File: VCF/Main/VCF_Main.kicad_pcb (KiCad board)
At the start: 2 copper layers, 39.6 x 74.4 mm, 46 parts, among them J1 Power, J2 Power, U1 TL072, U2 TL072, U3 AS3320

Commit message: Clean up VCF boards
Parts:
- added REF**: OSHW-Logo2_7.3x6mm_SilkScreen, Symbol:OSHW-Logo2_7.3x6mm_SilkScreen, B.Cu at (69.6, 102.4)
- moved J2 2.79 mm to (67.8, 126.0)
- moved R3 1.02 mm to (99.8, 131.8)
- moved R2 0.51 mm to (99.8, 129.8)
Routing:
- net +12V: track 80.9 -> 82.6 mm
- net -12V: track 149.0 -> 150.2 mm
- net /In_3: track 22.7 -> 21.6 mm
- net Net-(R1-Pad1): track 19.5 -> 18.9 mm
- net GNDREF: vias 0 -> 4
- net (no net): vias 4 -> 0
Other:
- board size 39.6 x 74.4 mm -> 39.6 x 75.2 mm
- board text added: "+12V"
- board text added: "-12V"
- board text added: "Cutoff"
- board text added: "CutoffM"
- board text added: "In 1"
- board text added: "In 2"
- board text added: "In 3"
- board text added: "Out"
- board text added: "Res"
- board text added: "ResM"
- board text added: "VCF Main Board Rev 2"
- board text added: "WH"
- board text removed: "VCF Board Rev 2"
- board text removed: "WHSynth"

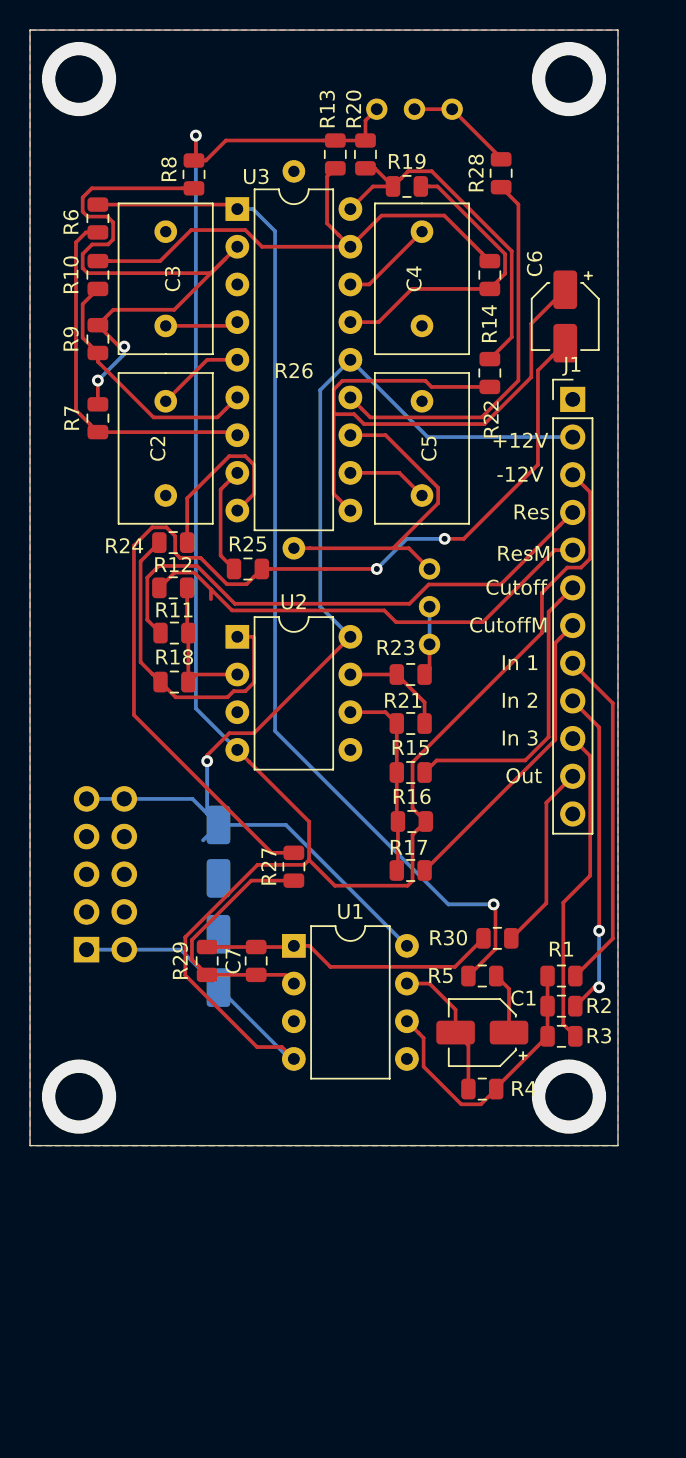
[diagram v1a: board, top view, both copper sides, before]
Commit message: Fix inverted resonance control input
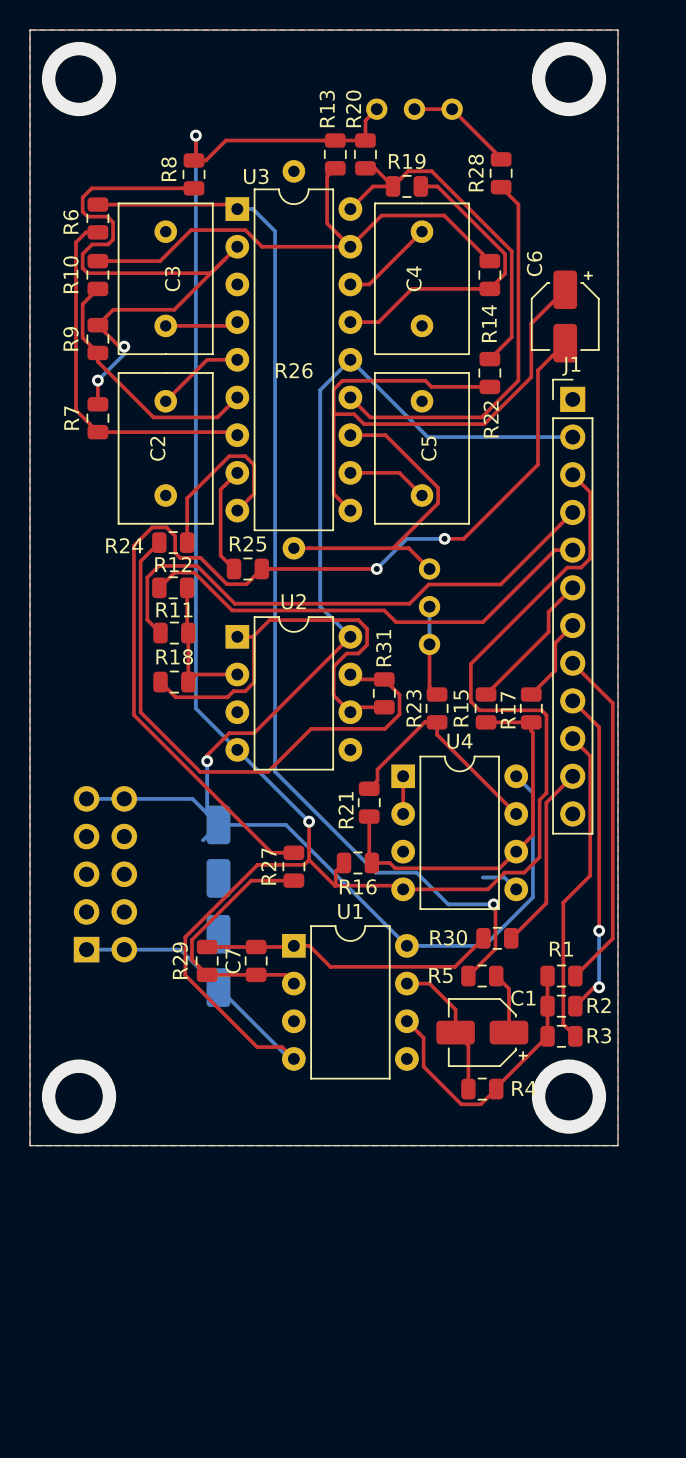
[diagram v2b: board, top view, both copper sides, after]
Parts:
- added R31: 100K, Resistor_SMD:R_0805_2012Metric, F.Cu at (87.9, 108.7)
- added U4: TL072, Package_DIP:DIP-8_W7.62mm, F.Cu at (89.2, 114.3)
- moved R17 13.6 mm to (97.8, 109.7), turned to 90 degrees
- moved R15 6.67 mm to (94.7, 109.7), turned to 90 degrees
- moved R21 6.02 mm to (86.9, 116.1), turned to 270 degrees
- moved R16 4.58 mm to (86.1, 120.1), turned to 180 degrees
- moved R23 2.90 mm to (91.4, 109.7), turned to 270 degrees
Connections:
- R24 pad 2: Net-(R18-Pad1) -> Net-(R24-Pad2)
- U2 pad 6: Net-(R15-Pad1) -> Net-(R18-Pad1)
- U2 pad 7: Net-(R21-Pad1) -> Net-(R24-Pad2)
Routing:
- net Net-(R24-Pad2): track 0.00 -> 37.9 mm
- net +12V: track 82.6 -> 101.1 mm
- net /Cutoff_Mod: track 20.6 -> 5.81 mm
- net Net-(R15-Pad1): track 13.4 -> 25.8 mm
- net -12V: track 150.2 -> 162.5 mm, vias 1 -> 2
- net /Cutoff: track 20.1 -> 9.61 mm
- net Net-(R21-Pad1): track 7.21 -> 15.2 mm
- net Net-(R18-Pad1): track 21.9 -> 29.7 mm
- net GNDREF: track 0.00 -> 2.58 mm
- net Net-(U4-Pad1): track 0.00 -> 2.54 mm
- net Net-(R5-Pad1): track 71.6 -> 73.2 mm
- net Net-(R23-Pad1): track 4.71 -> 6.13 mm
- net /Res_Mod: track 32.3 -> 31.7 mm
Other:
- board text removed: "+12V"
- board text removed: "-12V"
- board text removed: "Cutoff"
- board text removed: "CutoffM"
- board text removed: "In 1"
- board text removed: "In 2"
- board text removed: "In 3"
- board text removed: "Out"
- board text removed: "Res"
- board text removed: "ResM"

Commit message: Bunch of bug fixes and tweaks
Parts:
- added C10: C, Capacitor_SMD:C_0805_2012Metric, F.Cu at (91.9, 136.0)
- added C11: C, Capacitor_SMD:C_0805_2012Metric, F.Cu at (71.0, 106.3)
- added C12: C, Capacitor_SMD:C_0805_2012Metric, F.Cu at (83.4, 116.1)
- added C13: C, Capacitor_SMD:C_0805_2012Metric, F.Cu at (73.8, 111.4)
- added H1: Top_MH1, Eurorack:eurorack_mounting_hole, F.Cu at (67.3, 67.3)
- added H2: Bottom_MH1, Eurorack:eurorack_mounting_hole, F.Cu at (67.3, 135.9)
- added H3: Top_MH2, Eurorack:eurorack_mounting_hole, F.Cu at (100.3, 67.3)
- added H4: Bottom_MH2, Eurorack:eurorack_mounting_hole, F.Cu at (100.3, 135.9)
- moved R4 1.20 mm to (95.5, 136.0), turned to 270 degrees
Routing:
- net Net-(C11-Pad2): track 29.7 -> 35.3 mm
- net Net-(C13-Pad2): track 37.9 -> 42.9 mm
- net Net-(C11-Pad1): track 9.89 -> 14.1 mm
- net Net-(C12-Pad2): track 15.2 -> 18.7 mm
- net Net-(C1-Pad2): track 9.72 -> 13.0 mm
- net Net-(C10-Pad1): track 18.9 -> 21.3 mm
- net Net-(C6-Pad2): track 68.3 -> 70.4 mm
- net GNDREF: vias 4 -> 0

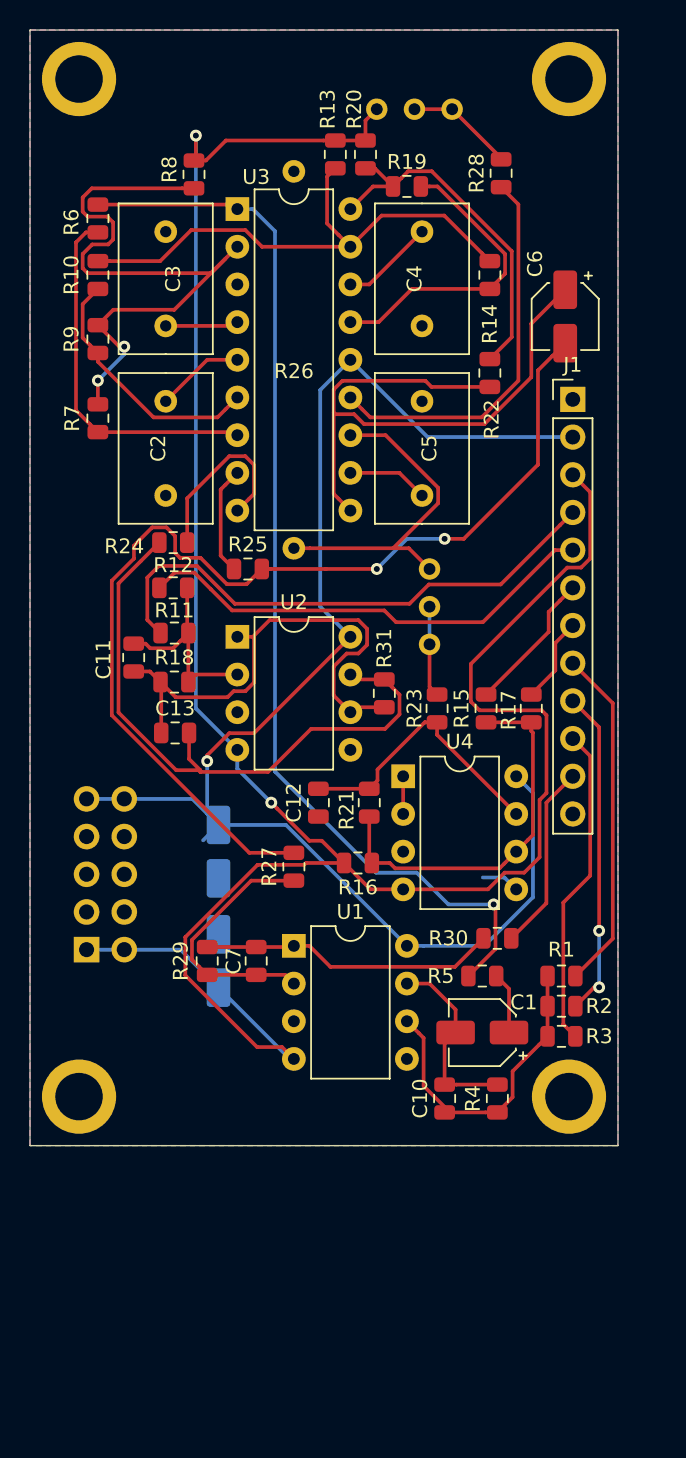
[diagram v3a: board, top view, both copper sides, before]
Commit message: Clean up layout of VCF board
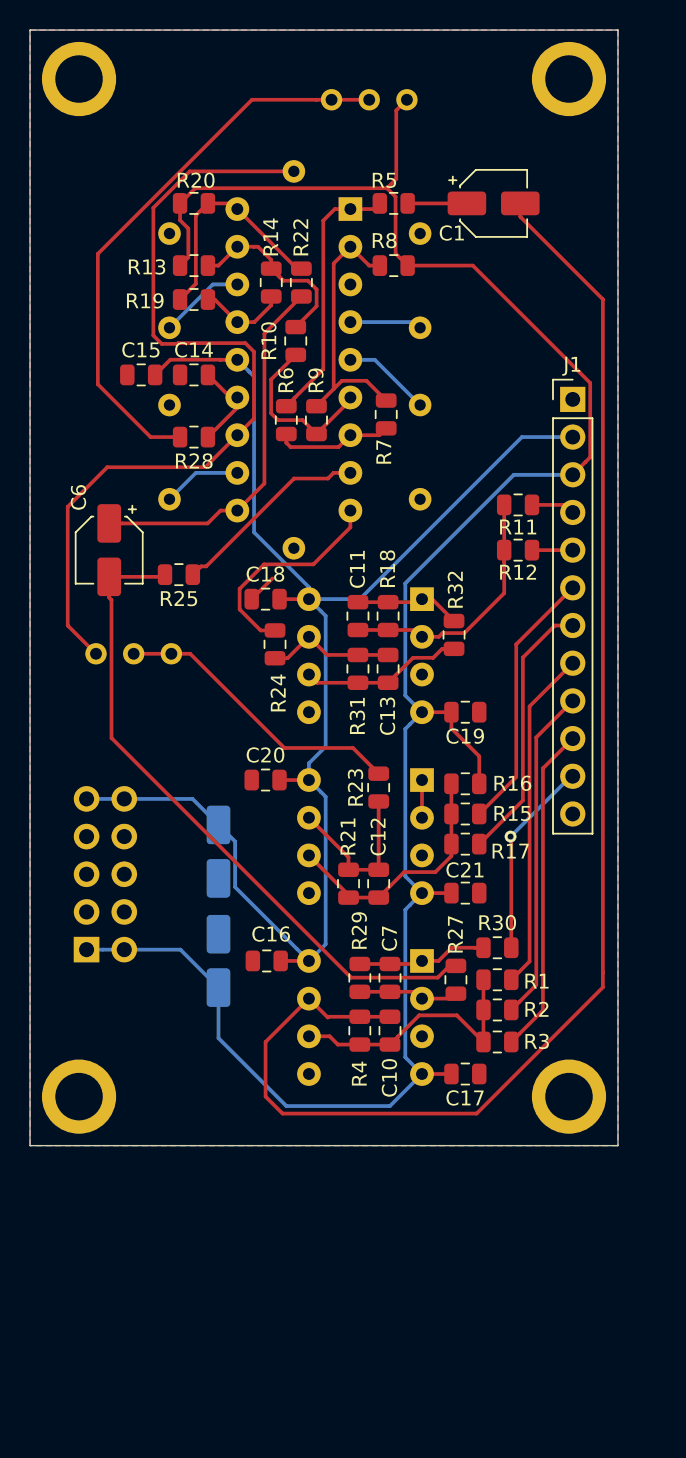
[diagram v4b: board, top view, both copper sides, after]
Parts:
- added C14: 0.1uF, Capacitor_SMD:C_0805_2012Metric, F.Cu at (75.1, 87.2)
- added C15: 0.1uF, Capacitor_SMD:C_0805_2012Metric, F.Cu at (71.5, 87.2)
- added C16: 0.1uF, Capacitor_SMD:C_0805_2012Metric, F.Cu at (80.0, 126.7)
- added C17: 0.1uF, Capacitor_SMD:C_0805_2012Metric, F.Cu at (93.3, 134.4)
- added C18: 0.1uF, Capacitor_SMD:C_0805_2012Metric, F.Cu at (79.9, 102.4)
- added C19: 0.1uF, Capacitor_SMD:C_0805_2012Metric, F.Cu at (93.3, 110.0)
- added C20: 0.1uF, Capacitor_SMD:C_0805_2012Metric, F.Cu at (79.9, 114.6)
- added C21: 0.1uF, Capacitor_SMD:C_0805_2012Metric, F.Cu at (93.3, 122.2)
- added R32: 100K, Resistor_SMD:R_0805_2012Metric, F.Cu at (92.6, 104.8)
- C2, C3, C4, C5, R26, U1, U2, U3, U4: moved to B.Cu
- R17: value 100K -> 200K
- moved C1 55.9 mm to (95.2, 75.7), turned to 0 degrees
- moved R5 52.4 mm to (88.5, 75.7)
- moved REF** 34.7 mm to (76.5, 68.3)
- moved C6 34.5 mm to (69.3, 99.1)
- moved R28 27.3 mm to (75.1, 91.4), turned to 180 degrees
- moved R11 24.7 mm to (96.9, 96.0), turned to 0 degrees
- moved R12 23.4 mm to (96.9, 99.1), turned to 0 degrees
- moved RV6 23.2 mm to (68.5, 106.0), turned to 180 degrees
- moved R7 19.4 mm to (88.0, 89.9)
- moved R6 18.6 mm to (81.3, 90.3)
- moved C2 17.1 mm to (90.3, 92.5)
- moved C3 17.1 mm to (90.3, 80.9)
- moved C5 17.0 mm to (73.4, 92.5)
- moved C4 17.0 mm to (73.4, 80.9), turned to 90 degrees
- moved R19 16.2 mm to (75.1, 82.2)
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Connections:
- C13 pad 1: Net-(C11-Pad2) -> Net-(C13-Pad1)
- R31 pad 2: Net-(C11-Pad2) -> Net-(C13-Pad1)
- U2 pad 6: Net-(C11-Pad2) -> Net-(C13-Pad1)
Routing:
- net Net-(C1-Pad2): track 13.0 -> 95.7 mm
- net Net-(R5-Pad1): track 73.2 -> 17.8 mm, vias 1 -> 0
- net Net-(C13-Pad2): track 42.9 -> 8.72 mm
- net Net-(R26-Pad1): track 22.4 -> 56.6 mm
- net /Res: track 36.7 -> 2.96 mm
- net Net-(R28-Pad2): track 7.29 -> 38.4 mm
- net /Res_Mod: track 31.7 -> 2.75 mm
- net Net-(C11-Pad2): track 35.3 -> 7.17 mm
- net Net-(R7-Pad1): track 44.4 -> 18.5 mm, vias 2 -> 0
- net Net-(C6-Pad2): track 70.4 -> 45.0 mm, vias 2 -> 0
- net Net-(R10-Pad1): track 36.1 -> 12.5 mm
- net Net-(C14-Pad2): track 26.4 -> 6.10 mm
- net -12V: track 162.0 -> 144.7 mm, vias 2 -> 0
- net Net-(R6-Pad1): track 24.6 -> 7.96 mm
- net Net-(C6-Pad1): track 41.3 -> 25.2 mm
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
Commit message: Make VCF front panel bigger. Re-align IO and FP boards.
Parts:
- moved H1 23.2 mm to (80.5, 86.4)
- moved C1 19.2 mm to (97.8, 94.7)
- moved C10 19.2 mm to (90.8, 150.5)
- moved C11 19.2 mm to (88.6, 122.6)
- moved C18 19.2 mm to (82.4, 121.4)
- moved C19 19.2 mm to (95.9, 129.0)
- moved C20 19.2 mm to (82.4, 133.6)
- moved C8 19.2 mm to (79.2, 138.4)
- moved H4 19.2 mm to (102.9, 154.9)
- moved R26 19.2 mm to (84.3, 104.0)
- moved R27 19.2 mm to (95.2, 147.1)
- moved U3 19.2 mm to (88.1, 95.1)
- moved C14 19.2 mm to (77.6, 106.3)
- moved C15 19.2 mm to (74.0, 106.3)
- moved H2 19.2 mm to (69.8, 154.9)
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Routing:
- net GNDREF: track 1.98 -> 4.30 mm
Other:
- board text added: "Freq. CV Rej."
- board text added: "Freq. Scale"
